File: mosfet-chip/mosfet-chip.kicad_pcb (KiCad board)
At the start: 2 copper layers, 33.7 x 17.1 mm, 8 parts, among them J1 Conn_01x02, J2 Screw_Terminal_01x02, J3 Screw_Terminal_01x02, Q1 IRLZ24

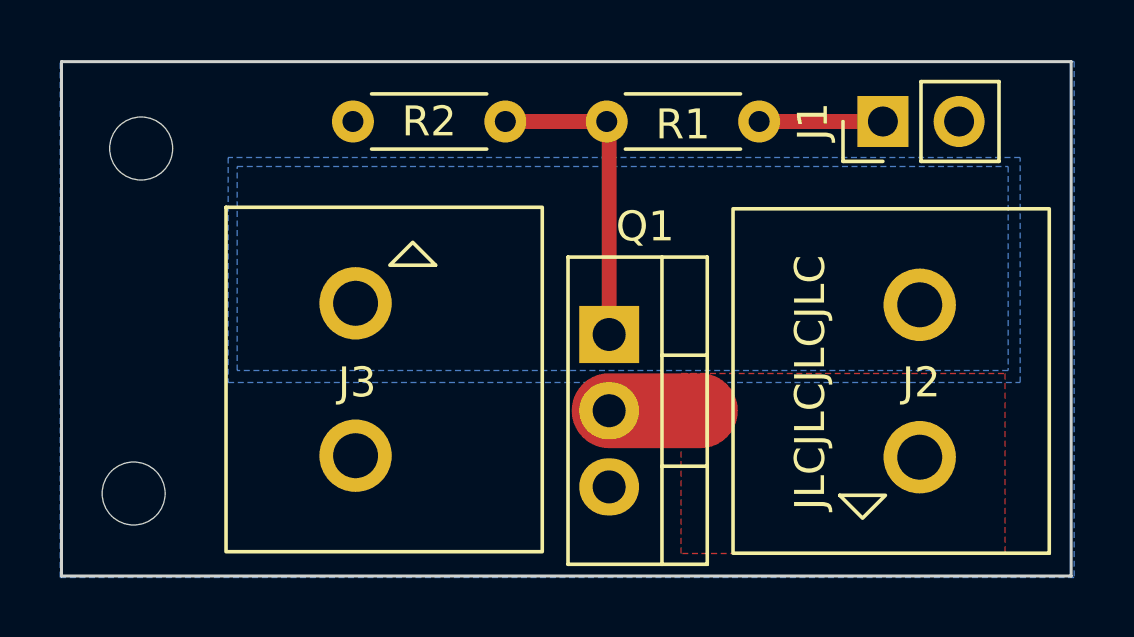
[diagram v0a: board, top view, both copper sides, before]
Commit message: Add LED; use SMT for passives; fill zones.
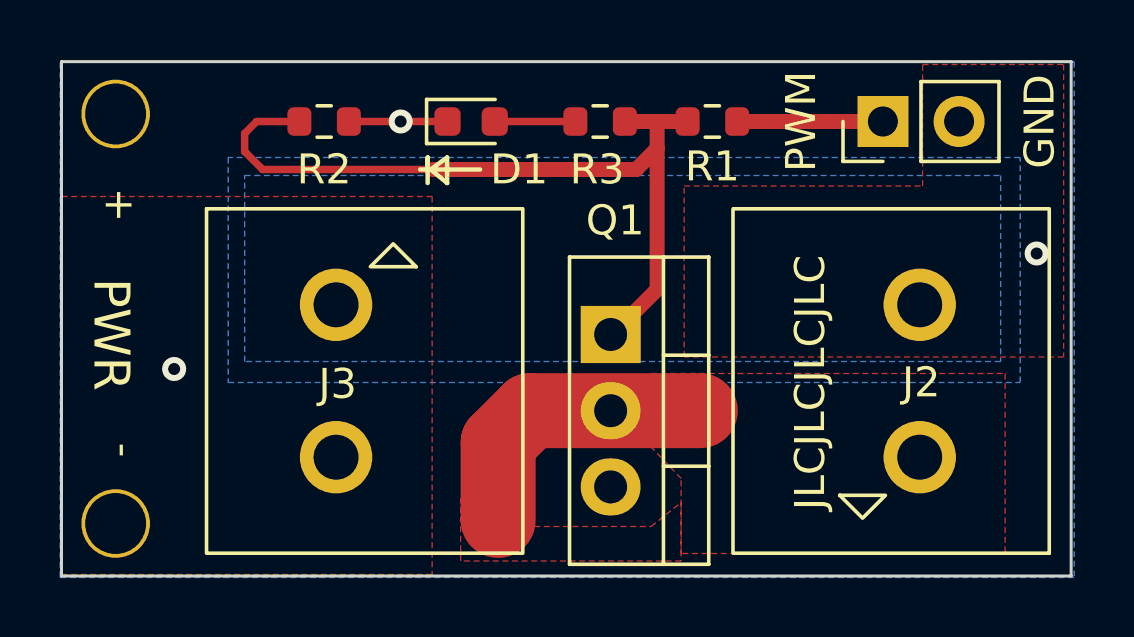
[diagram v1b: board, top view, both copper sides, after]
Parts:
- added D1: XL-1608SURC-06, LED_SMD:LED_0603_1608Metric, F.Cu at (67.5, 59.6)
- added R3: 3K3, Resistor_SMD:R_0603_1608Metric, F.Cu at (71.8, 59.6)
- H1, H2: footprint MountingHole:MountingHole_2.1mm -> Aaron_Pads:MountingHole_80mil
- Q1: value IRLZ24 -> IRLZ44
- R1, R2: footprint Resistor_THT:R_Axial_DIN0204_L3.6mm_D1.6mm_P5.08mm_Horizontal -> Resistor_SMD:R_0603_1608Metric
- moved R1 1.56 mm to (75.5, 59.6)
- moved H1 1.43 mm to (55.7, 59.3)
- moved H2 1.17 mm to (55.7, 73.0)
- moved R2 0.96 mm to (62.6, 59.6), turned to 180 degrees
- moved J3 0.65 mm to (63.0, 65.7)
- moved Q1 0.05 mm to (72.2, 66.7)
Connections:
- net Net-(Q1-Pad1) renamed /GATE
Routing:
- net /GATE: track 10.6 -> 26.7 mm
- net /LOAD-: track 3.04 -> 9.78 mm
- net GND: track 0.00 -> 3.29 mm, vias 0 -> 3
- net Net-(D1-Pad2): track 0.00 -> 2.69 mm
- net /SIGNAL: track 4.20 -> 4.86 mm
- added copper zone on F.Cu, net GND
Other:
- board text added: "${board_name}"
- board text added: "(N-MOS)"
- board text added: "+"
- board text added: "-"
- board text added: "GND"
- board text added: "LOAD"
- board text added: "PWM"
- board text added: "PWR"
- board text added: "v${rev}"

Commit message: Update part numbers for JLC assembly.
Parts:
- Q1: value IRLZ44 -> IRLZ34
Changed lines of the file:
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@@
     (descr "Through hole straight pin header, 1x02, 2.54mm pitch, single row")
     (tags "Through hole pin header THT 1x02 2.54mm single row")
+    (property "MANUFACTURER" "TE Connectivity AMP Connectors")
+    (property "MPN" "5-146858-1")
+    (property "SPN" "A105469CT-ND")
     (property "Sheetfile" "mosfet-chip.kicad_sch")
     (property "Sheetname" "")
@@
     (tags "TO-220-3 Vertical RM 2.54mm")
     (property "MANUFACTURER" "Infineon")
-    (property "MPN" "IRLZ44NPbF")
-    (property "SPN" "IRLZ44NPBF-ND")
+    (property "MPN" "IRLZ34NPbF")
+    (property "SPN" "IRLZ34NPBF-ND")
     (property "Sheetfile" "mosfet-chip.kicad_sch")
     (property "Sheetname" "")
@@
       (effects (font (size 1 1) (thickness 0.15)))
     )
-    (fp_text value "IRLZ44" (at 2.54 2.5 -90) (layer "F.Fab")
+    (fp_text value "IRLZ34" (at 2.54 2.5 -90) (layer "F.Fab")
       (effects (font (size 1 1) (thickness 0.15)))
     )
@@
     (pts (xy 87.500003 57.60499) (xy 87.500003 74.74999))
     (height -5.299997)
-    (gr_text "675.0000 mils" (at 91.65 66.17749 90) (layer "Dwgs.User")
+    (gr_text "17.1450 mm" (at 91.65 66.17749 90) (layer "Dwgs.User")
       (effects (font (size 1 1) (thickness 0.15)))
     )
@@
     (pts (xy 53.845003 74.74999) (xy 87.500003 74.74999))
     (height 6.35001)
-    (gr_text "1325.0000 mils" (at 70.672503 79.95) (layer "Dwgs.User")
-      (effects (font (size 1 1) (thickness 0.15)))
-    )
+    (gr_text "33.6550 mm" (at 70.672503 79.95) (layer "Dwgs.User")
+      (effects (font (size 1 1) (thickness 0.15)))
+    )

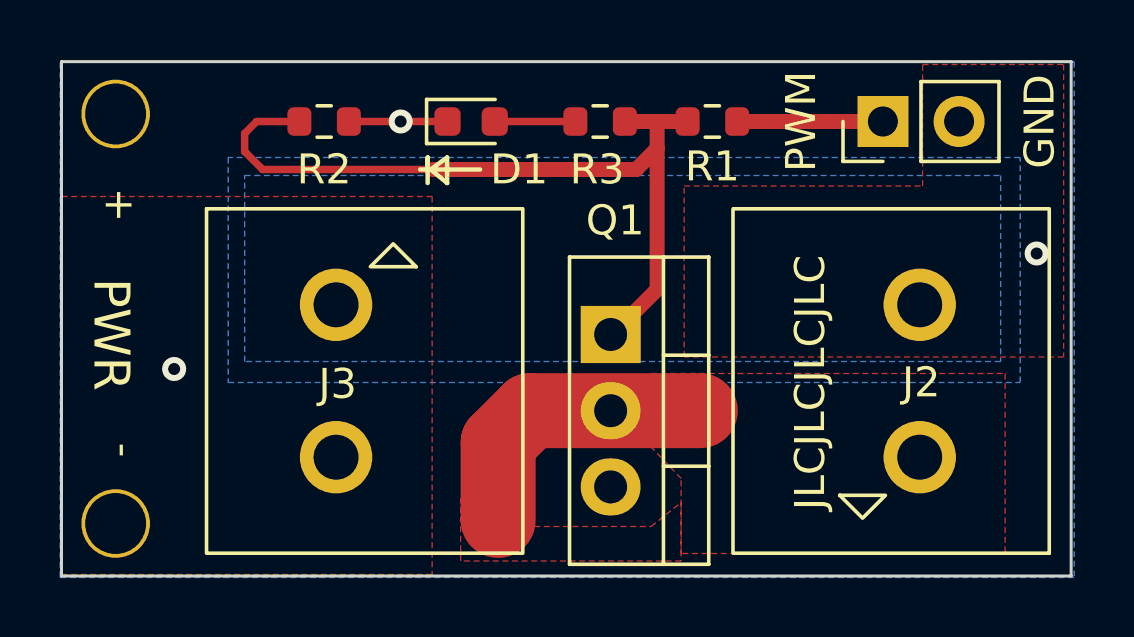
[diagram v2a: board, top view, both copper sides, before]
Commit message: MOSFET Chip ready for RTM.
* Change screw terminal to Phoenix Contact MPN 1711725.
* Add appropriately-sized thermal reliefs to pads in pour zones.
* VArious small tweaks, silkscreen adjustments, etc.
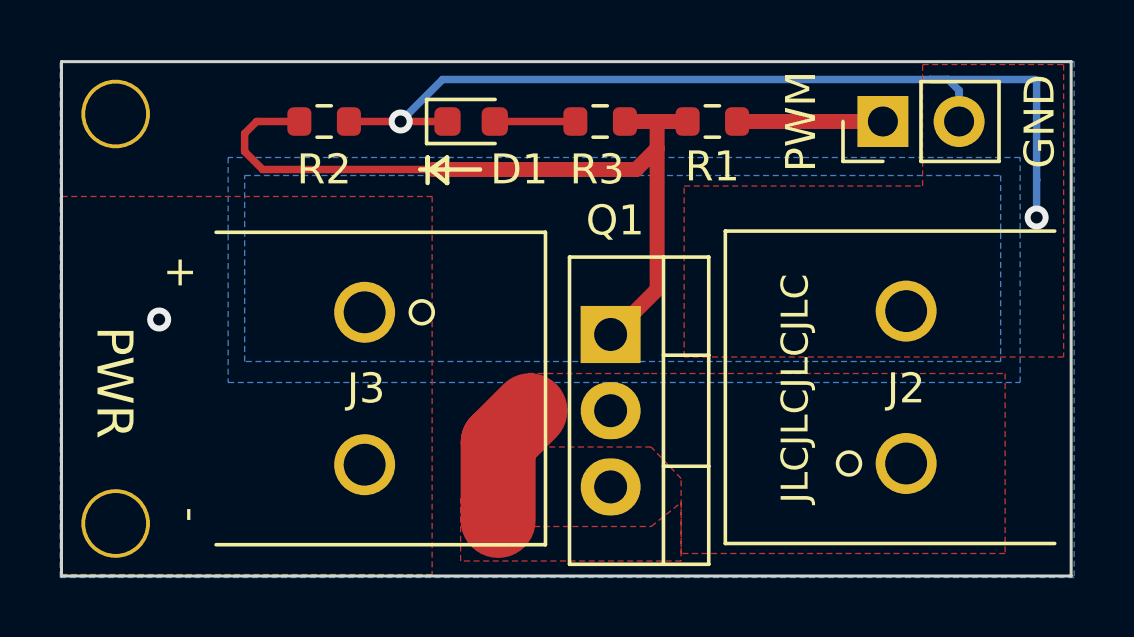
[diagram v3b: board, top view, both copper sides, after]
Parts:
- J2, J3: footprint Aaron_THT:AdamTech_EB147A-02-D -> Aaron_Phoenix_Parts:Phoenix_1x02_1711725
- moved J3 0.98 mm to (64.0, 66.0), turned to -90 degrees
- moved J2 0.50 mm to (82.0, 71.0), turned to 90 degrees
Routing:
- net GND: track 3.29 -> 31.8 mm
- net /LOAD-: track 9.78 -> 4.10 mm
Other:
- board text added: "(${FET_PART})"
- board text removed: "(N-MOS)"

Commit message: Update board for D4M.
* Fix layout violation: Move SMT components 2.5mm+ from edge.
* Update MPN/SPNs for resistors to use correct JLC basic library parts.
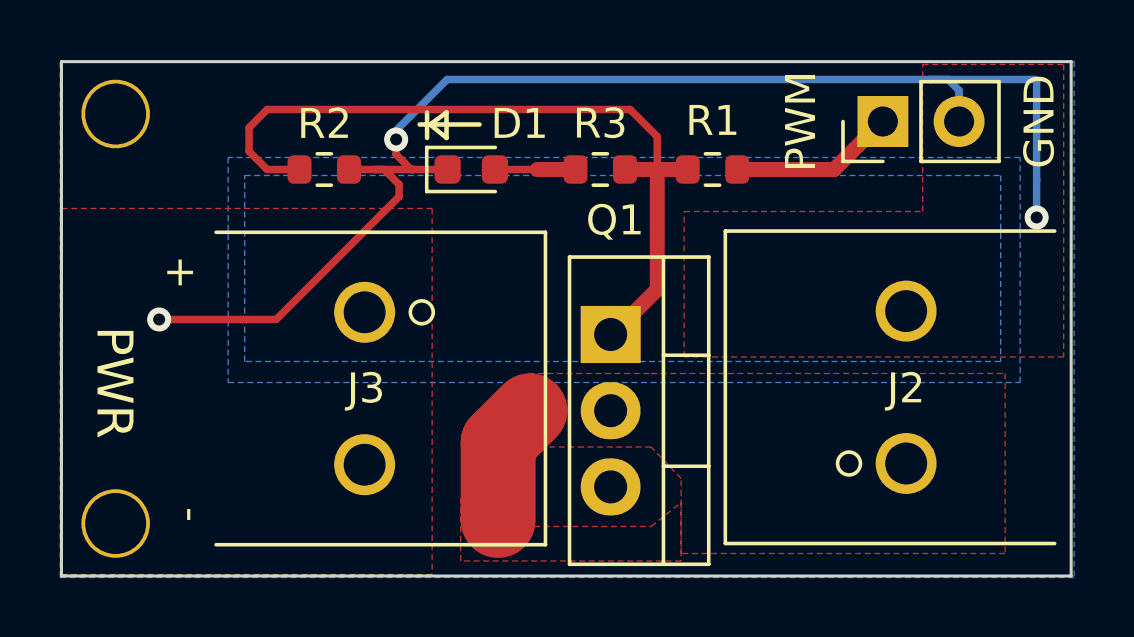
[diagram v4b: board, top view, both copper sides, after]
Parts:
- moved D1 1.60 mm to (67.5, 61.2)
- moved R1 1.60 mm to (75.5, 61.2)
- moved R2 1.60 mm to (62.6, 61.2)
- moved R3 1.60 mm to (71.8, 61.2)
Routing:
- net GND: track 31.8 -> 44.8 mm
- net Net-(D1-Pad2): track 2.69 -> 3.89 mm
- net /SIGNAL: track 4.86 -> 5.49 mm
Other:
- board text removed: "JLCJLCJLCJLC"
